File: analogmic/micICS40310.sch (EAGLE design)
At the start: 3 parts

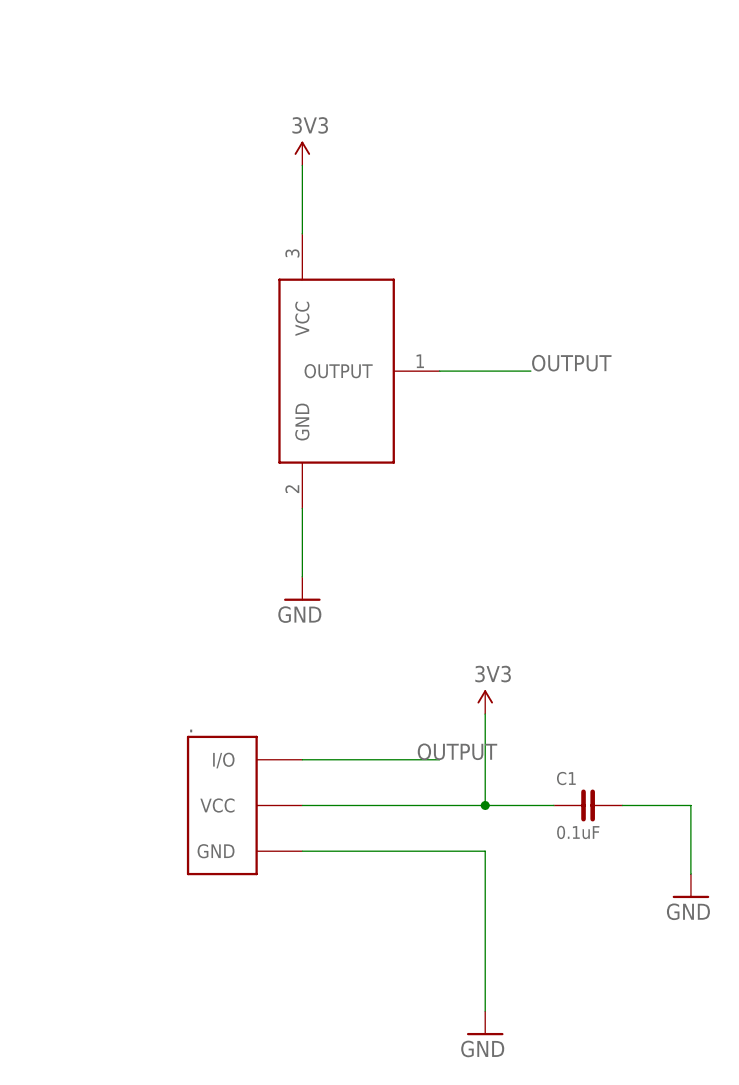
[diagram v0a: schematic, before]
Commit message: Update opamp.
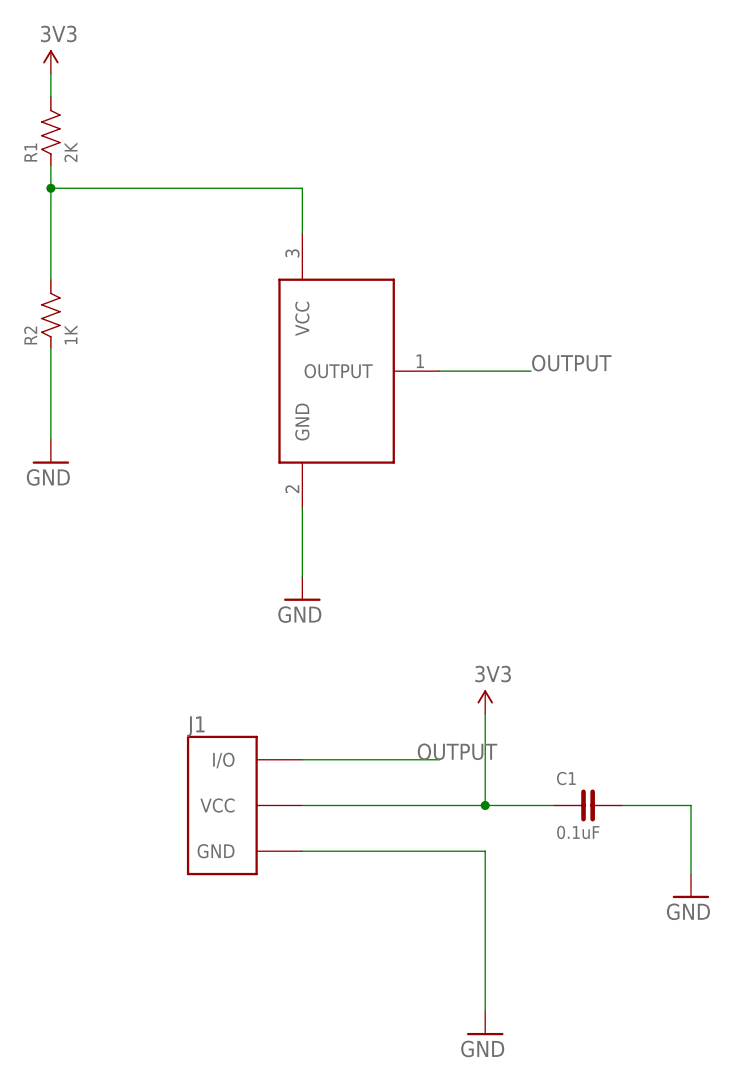
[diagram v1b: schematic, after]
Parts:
- removed .: (no value), FaBo-Template:FABO_BRICK_3PIN-S03B-PASK-2
- added J1: (no value), FaBo-Template:FABO_BRICK_3PIN-03B-PASK-1_NAME_BOTTOM
- added R1: 2K, FaBo-Resistors:RESISTOR-0603
- added R2: 1K, FaBo-Resistors:RESISTOR-0603
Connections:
- new net N$1: ICS40310.VCC, R1.1, R2.2
- net 3V3: now also J1.VCC, R1.2; no longer ..VCC, ICS40310.VCC
- net GND: now also J1.GND, R2.1; no longer ..GND
- net OUTPUT: now also J1.I/O; no longer ..I/O
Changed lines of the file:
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@@
 <part name="C1" library="FaBo-Capacitor" deviceset="CAPACITOR" device="-0603" value="0.1uF"/>
 <part name="GND3" library="FaBo-Supply" deviceset="GND" device=""/>
-<part name="." library="FaBo-Template" deviceset="FABO_BRICK_3PIN" device="-S03B-PASK-2"/>
 <part name="ICS40310" library="FaBo-Sound" deviceset="ANALOG-MIC" device="ICS40310"/>
+<part name="R1" library="FaBo-Resistors" deviceset="RESISTOR" device="-0603" value="2K"/>
+<part name="R2" library="FaBo-Resistors" deviceset="RESISTOR" device="-0603" value="1K"/>
+<part name="GND4" library="FaBo-Supply" deviceset="GND" device=""/>
+<part name="J1" library="FaBo-Template" deviceset="FABO_BRICK_3PIN" device="-03B-PASK-1_NAME_BOTTOM"/>
 </parts>
 <sheets>
@@
 <instances>
 <instance part="U$1" gate="G$1" x="0" y="0" smashed="yes"/>
-<instance part="3V1" gate="G$1" x="55.88" y="154.94" smashed="yes">
-<attribute name="VALUE" x="54.61" y="158.496" size="1.778" layer="96"/>
+<instance part="3V1" gate="G$1" x="27.94" y="165.1" smashed="yes">
+<attribute name="VALUE" x="26.67" y="168.656" size="1.778" layer="96"/>
 </instance>
 <instance part="3V2" gate="G$1" x="76.2" y="93.98" smashed="yes">
@@
 <attribute name="VALUE" x="96.266" y="71.12" size="1.778" layer="96"/>
 </instance>
-<instance part="." gate="G$1" x="48.26" y="83.82" smashed="yes">
+<instance part="ICS40310" gate="G$1" x="55.88" y="132.08" smashed="yes"/>
+<instance part="R1" gate="G$1" x="27.94" y="157.48" smashed="yes" rot="R90">
+<attribute name="NAME" x="26.416" y="155.194" size="1.4224" layer="95" rot="R90"/>
+<attribute name="VALUE" x="29.464" y="155.194" size="1.4224" layer="96" rot="R90" align="top-left"/>
+</instance>
+<instance part="R2" gate="G$1" x="27.94" y="137.16" smashed="yes" rot="R90">
+<attribute name="NAME" x="26.416" y="134.874" size="1.4224" layer="95" rot="R90"/>
+<attribute name="VALUE" x="29.464" y="134.874" size="1.4224" layer="96" rot="R90" align="top-left"/>
+</instance>
+<instance part="GND4" gate="G$1" x="27.94" y="124.46" smashed="yes">
+<attribute name="VALUE" x="25.146" y="119.38" size="1.778" layer="96"/>
+</instance>
+<instance part="J1" gate="G$1" x="48.26" y="83.82" smashed="yes">
 <attribute name="NAME" x="43.18" y="91.948" size="1.778" layer="95"/>
 </instance>
-<instance part="ICS40310" gate="G$1" x="55.88" y="132.08" smashed="yes"/>
 </instances>
 <busses>
@@
 <wire x1="55.88" y1="88.9" x2="71.12" y2="88.9" width="0.1524" layer="91"/>
 <label x="68.58" y="88.9" size="1.778" layer="95"/>
-<pinref part="." gate="G$1" pin="I/O"/>
+<pinref part="J1" gate="G$1" pin="I/O"/>
 </segment>
 </net>
 <net name="3V3" class="0">
-<segment>
-<wire x1="55.88" y1="147.32" x2="55.88" y2="154.94" width="0.1524" layer="91"/>
-<pinref part="3V1" gate="G$1" pin="3V3"/>
-<pinref part="ICS40310" gate="G$1" pin="VCC"/>
-</segment>
 <segment>
 <wire x1="55.88" y1="83.82" x2="76.2" y2="83.82" width="0.1524" layer="91"/>
@@
 <wire x1="83.82" y1="83.82" x2="76.2" y2="83.82" width="0.1524" layer="91"/>
 <junction x="76.2" y="83.82"/>
-<pinref part="." gate="G$1" pin="VCC"/>
+<pinref part="J1" gate="G$1" pin="VCC"/>
+</segment>
+<segment>
+<pinref part="3V1" gate="G$1" pin="3V3"/>
+<pinref part="R1" gate="G$1" pin="2"/>
+<wire x1="27.94" y1="165.1" x2="27.94" y2="162.56" width="0.1524" layer="91"/>
 </segment>
 </net>
@@
 <wire x1="76.2" y1="78.74" x2="76.2" y2="60.96" width="0.1524" layer="91"/>
 <pinref part="GND2" gate="G$1" pin="GND"/>
-<pinref part="." gate="G$1" pin="GND"/>
+<pinref part="J1" gate="G$1" pin="GND"/>
 </segment>
 <segment>
@@
 <wire x1="99.06" y1="83.82" x2="99.06" y2="76.2" width="0.1524" layer="91"/>
 </segment>
+<segment>
+<pinref part="R2" gate="G$1" pin="1"/>
+<wire x1="27.94" y1="134.62" x2="27.94" y2="124.46" width="0.1524" layer="91"/>
+<pinref part="GND4" gate="G$1" pin="GND"/>
+</segment>
 </net>
+<net name="N$1" class="0">
+<segment>
+<pinref part="R1" gate="G$1" pin="1"/>
+<pinref part="R2" gate="G$1" pin="2"/>
+<wire x1="27.94" y1="154.94" x2="27.94" y2="152.4" width="0.1524" layer="91"/>
+<pinref part="ICS40310" gate="G$1" pin="VCC"/>
+<wire x1="27.94" y1="152.4" x2="27.94" y2="142.24" width="0.1524" layer="91"/>
+<wire x1="27.94" y1="152.4" x2="55.88" y2="152.4" width="0.1524" layer="91"/>
+<wire x1="55.88" y1="152.4" x2="55.88" y2="147.32" width="0.1524" layer="91"/>
+<junction x="27.94" y="152.4"/>
+</segment>
+</net>
